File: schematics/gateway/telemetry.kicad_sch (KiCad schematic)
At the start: 5 parts, among them J1 PZEM-004T, J2 Relay, J3 Bicolor LED, U2 SX1278

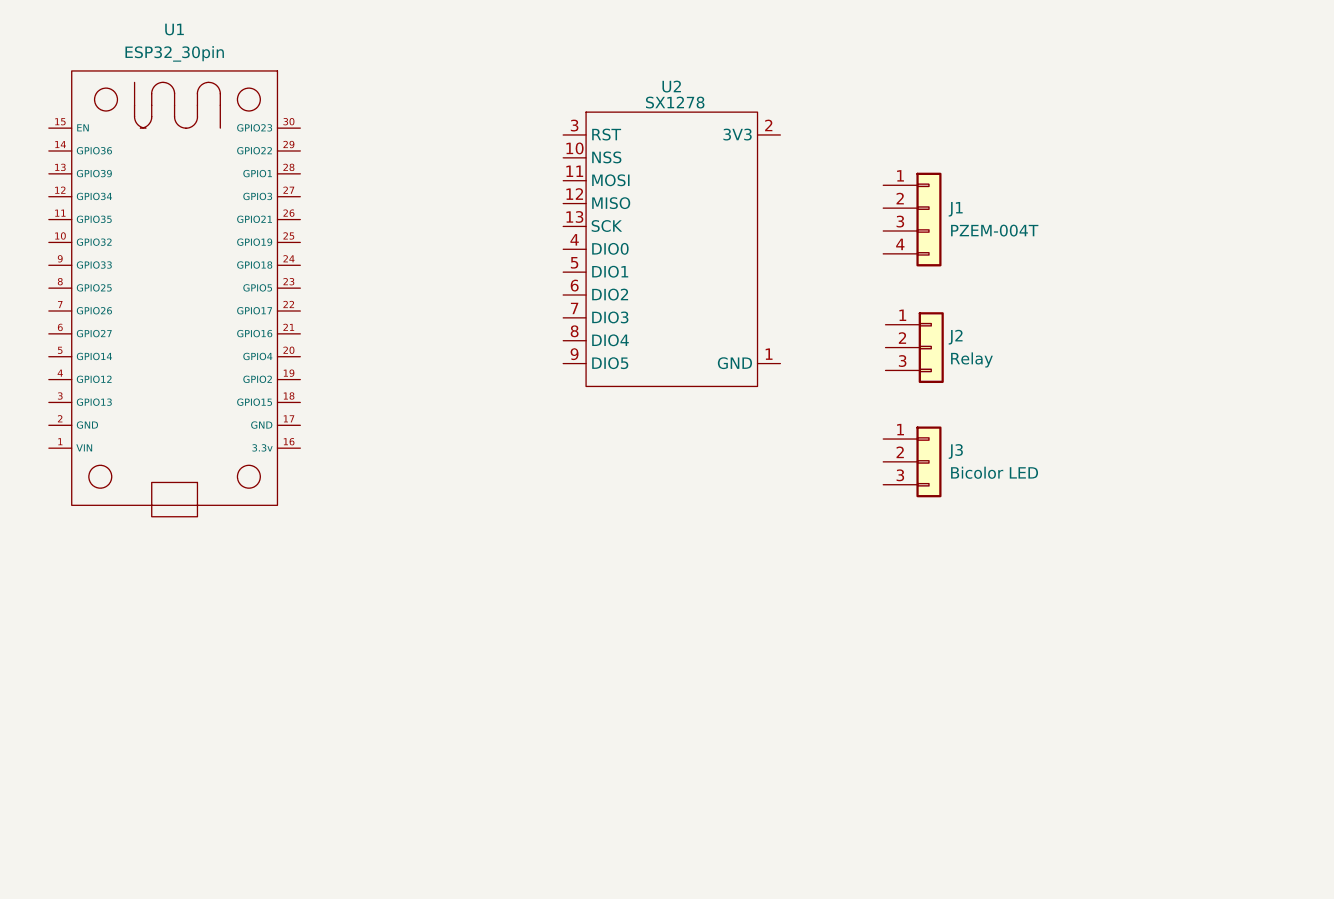
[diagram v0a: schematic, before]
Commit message: AP-STA fix + fake pzem mode
fix task starvation issue which prevented tasks from executing. create a testing module for LoRa connectivity
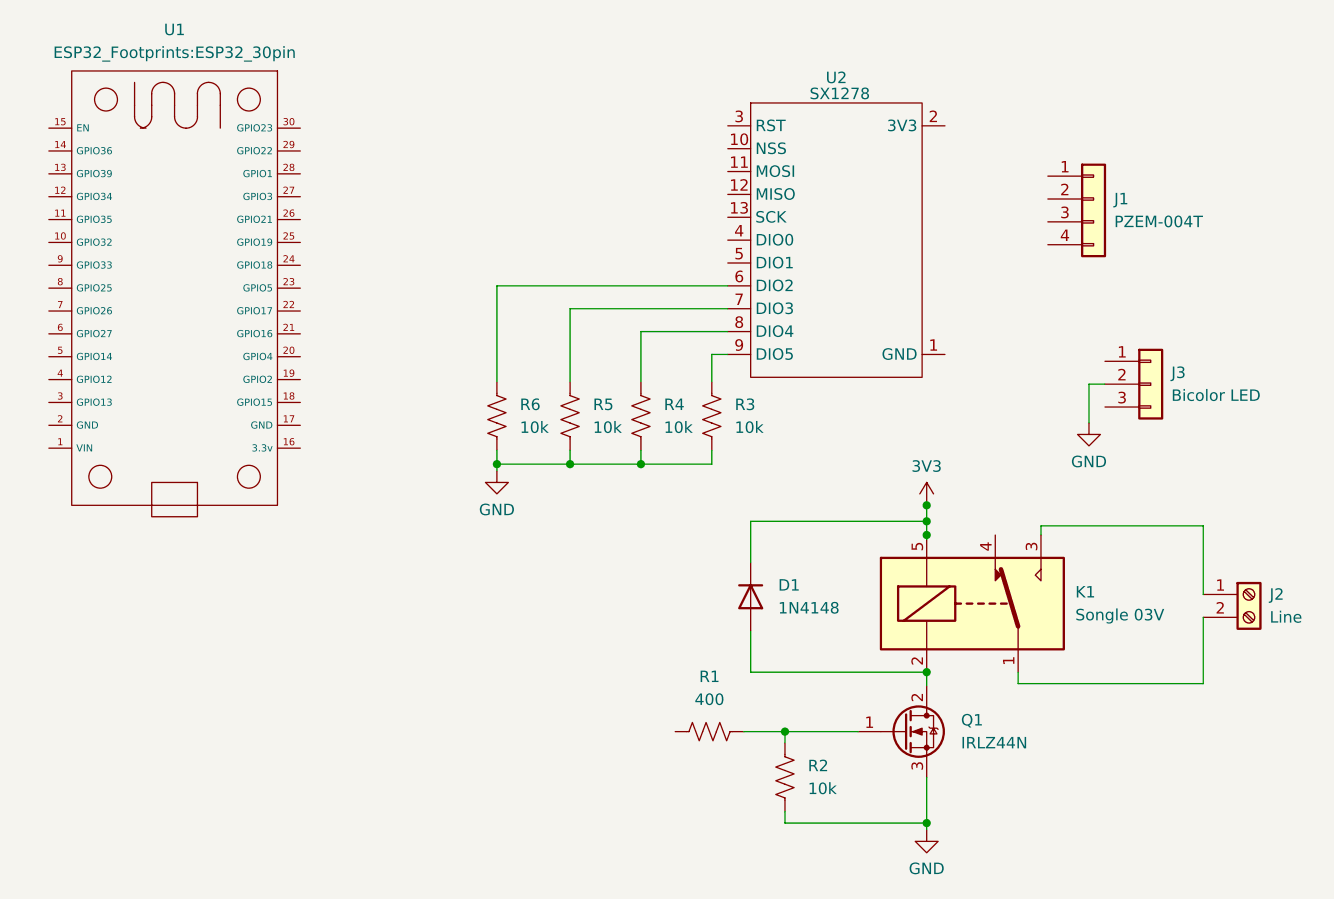
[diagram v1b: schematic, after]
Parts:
- removed J2: Relay, symbol Connector_Generic:Conn_01x03
- added D1: 1N4148, symbol Device:D
- added J2: Line, symbol Connector:Screw_Terminal_01x02
- added K1: Songle 03V, Relay_THT:Relay_SPDT_SANYOU_SRD_Series_Form_C, symbol Relay:SANYOU_SRD_Form_C
- added Q1: IRLZ44N, Package_TO_SOT_THT:TO-220-3_Vertical, symbol Transistor_FET:IRLZ44N
- added R1: 400, symbol Device:R_US
- added R2, R3, R4, R5, R6: 10k, symbol Device:R_US
- U1: footprint ESP32_30pin -> ESP32_Footprints:ESP32_30pin
- U2: footprint (none) -> LoRa_Breakout:LoRa-02
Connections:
- net GND: now reaches J3.2 (Pin_2)
- net GND: now also Q1.3 (S), R2.1, R3.1, R4.1, R5.1, R6.1
- net at U2.6 (DIO2): now also R6.2
- net at U2.7 (DIO3): now also R5.2
- net at U2.8 (DIO4): now also R4.2
- net at U2.9 (DIO5): now also R3.2
- new net: J2.2 (Pin_2), K1.1
- new net: D1.2 (A), K1.2, Q1.2 (D)
- new net: J2.1 (Pin_1), K1.3
- new net: Q1.1 (G), R1.2, R2.2
- new net 3V3: D1.1 (K), K1.5
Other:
- moved on the sheet: J1, J3, U2
